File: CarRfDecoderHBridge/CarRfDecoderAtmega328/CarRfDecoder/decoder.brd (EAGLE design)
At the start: 98.7 x 80 mm, 54 parts, among them U2 RFM69CW, U3 MCP73831, U4 ATMEGA328P, U6 MIC5219 3.3V, Y1 16MHZ

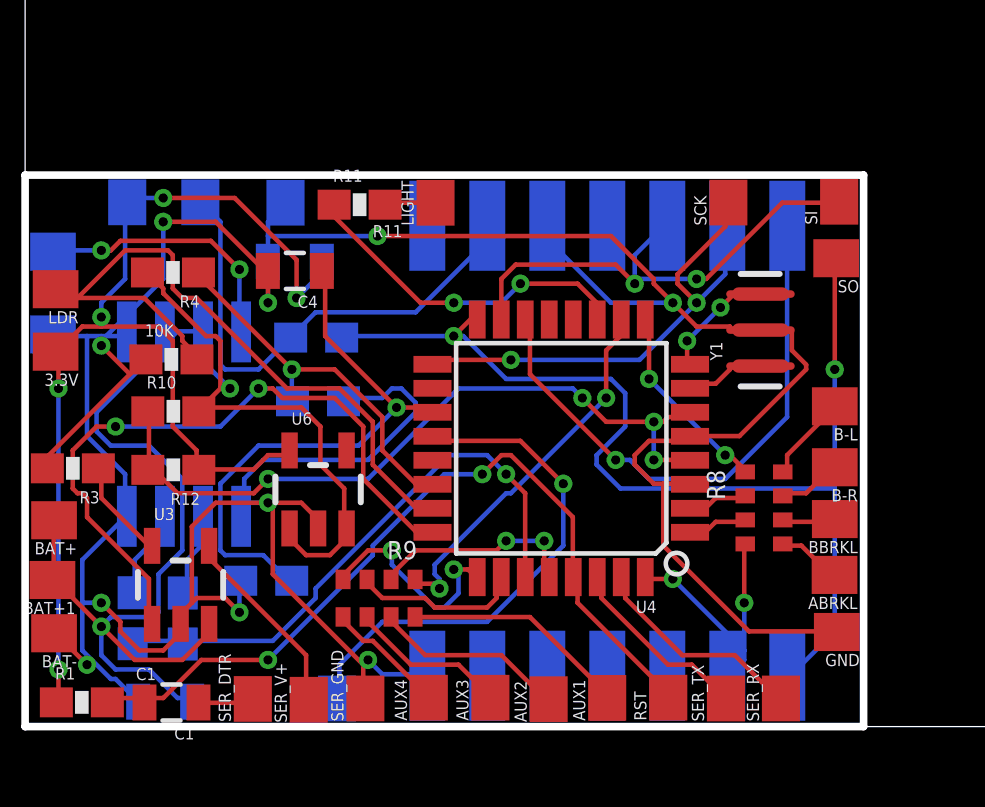
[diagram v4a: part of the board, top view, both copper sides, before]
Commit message: Change the pin to H-bridge to allow reverse control of the motor using A5
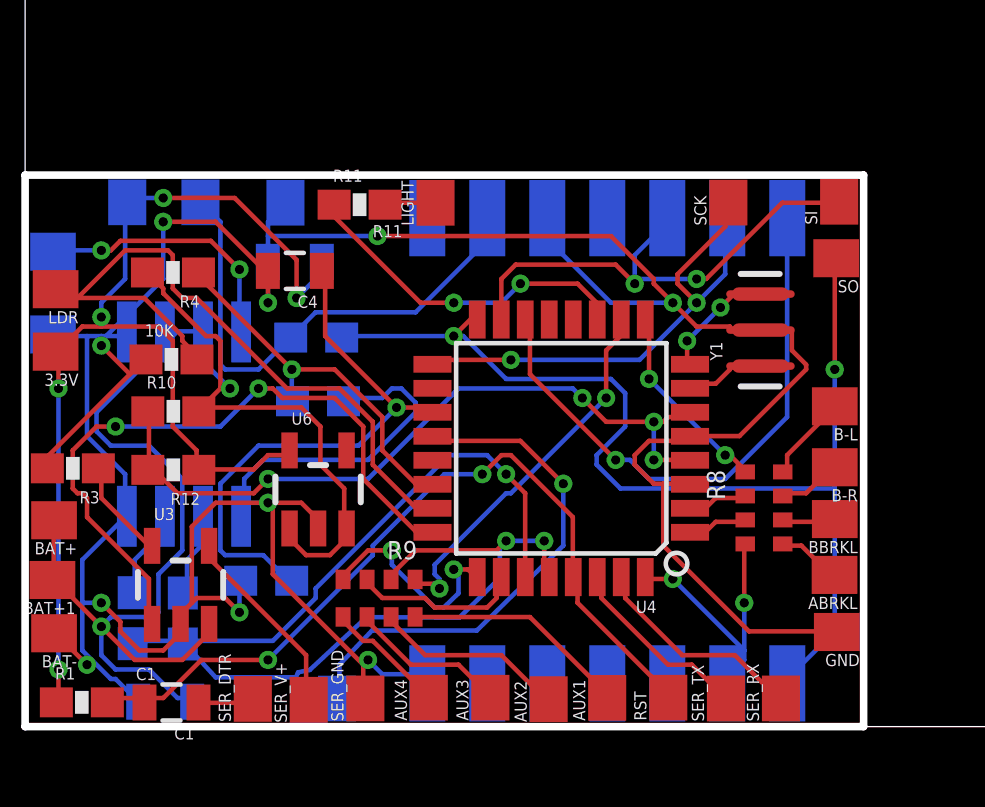
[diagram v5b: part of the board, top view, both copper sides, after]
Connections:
- net A4: no longer R6.1
- net A5: now also R6.1
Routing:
- net A5: track 7.00 -> 20.7 mm
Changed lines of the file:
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@@
 <wire x1="23.65375" y1="13.335" x2="22.86" y2="14.12875" width="0.1524" layer="1"/>
 <wire x1="24.765" y1="13.335" x2="23.65375" y2="13.335" width="0.1524" layer="1"/>
-<wire x1="18.7325" y1="16.66875" x2="18.6756" y2="16.6948" width="0.1524" layer="16"/>
+<wire x1="18.7325" y1="16.66875" x2="18.6756" y2="16.9488" width="0.1524" layer="16"/>
 <wire x1="24.765" y1="13.335" x2="24.765634375" y2="13.218053125" width="0.1524" layer="1"/>
 <wire x1="13.17625" y1="10.95375" x2="11.90625" y2="10.95375" width="0.1524" layer="16"/>
@@
 <wire x1="12.7" y1="2.2225" x2="13.17625" y2="1.74625" width="0.1524" layer="16"/>
 <wire x1="12.54125" y1="2.06375" x2="12.7" y2="2.2225" width="0.1524" layer="1"/>
-<wire x1="14.605" y1="1.74625" x2="14.6756" y2="1.6948" width="0.1524" layer="16"/>
+<wire x1="14.605" y1="1.74625" x2="14.6756" y2="1.4408" width="0.1524" layer="16"/>
 <wire x1="9.36625" y1="7.46125" x2="8.5725" y2="7.46125" width="0.1524" layer="16"/>
 <wire x1="8.5725" y1="7.46125" x2="8.4692625" y2="7.008784375" width="0.1524" layer="16"/>
@@
 <wire x1="19.20875" y1="8.09625" x2="17.78" y2="9.525" width="0.1524" layer="1"/>
 <wire x1="19.20875" y1="6.0325" x2="19.20875" y2="8.09625" width="0.1524" layer="16"/>
-<wire x1="16.66875" y1="3.4925" x2="19.20875" y2="6.0325" width="0.1524" layer="16"/>
-<wire x1="13.17625" y1="3.4925" x2="16.66875" y2="3.4925" width="0.1524" layer="16"/>
-<wire x1="11.7475" y1="2.06375" x2="13.17625" y2="3.4925" width="0.1524" layer="16"/>
+<wire x1="16.32493125" y1="3.201584375" x2="19.20875" y2="6.0325" width="0.1524" layer="16"/>
+<wire x1="12.83243125" y1="3.201584375" x2="16.32493125" y2="3.201584375" width="0.1524" layer="16"/>
+<wire x1="11.7475" y1="2.06375" x2="12.83243125" y2="3.201584375" width="0.1524" layer="16"/>
 <wire x1="11.7475" y1="0.9525" x2="11.7475" y2="2.06375" width="0.1524" layer="16"/>
 <wire x1="14.9225" y1="9.525" x2="14.84846875" y2="9.676678125" width="0.1524" layer="1"/>
@@
 <signal name="A4">
 <contactref element="U4" pad="27"/>
-<contactref element="R6" pad="1"/>
 <contactref element="R7" pad="1"/>
 <wire x1="6.50875" y1="2.8575" x2="4.92125" y2="2.8575" width="0.1524" layer="16"/>
 <wire x1="4.92125" y1="2.8575" x2="4.854525" y2="2.76374375" width="0.1524" layer="16"/>
-<wire x1="6.50875" y1="2.8575" x2="6.526196875" y2="2.753640625" width="0.1524" layer="16"/>
 <wire x1="17.93875" y1="7.77875" x2="17.93875" y2="5.08" width="0.1524" layer="1"/>
 <wire x1="17.30375" y1="8.41375" x2="17.93875" y2="7.77875" width="0.1524" layer="1"/>
@@
 <wire x1="6.6675" y1="2.8575" x2="9.525" y2="2.8575" width="0.1524" layer="16"/>
 <wire x1="17.93875" y1="5.08" x2="17.94106875" y2="4.984078125" width="0.1524" layer="1"/>
-<wire x1="6.6675" y1="2.8575" x2="6.526196875" y2="2.753640625" width="0.1524" layer="16"/>
 <via x="17.30375" y="8.41375" extent="1-16" drill="0.3048"/>
+<wire x1="6.50875" y1="2.8575" x2="6.6675" y2="2.8575" width="0" layer="19" extent="16-16"/>
 </signal>
 <signal name="A5">
@@
 <via x="17.30375" y="6.19125" extent="1-16" drill="0.3048"/>
 <via x="18.57375" y="6.19125" extent="1-16" drill="0.3048"/>
+<contactref element="R6" pad="1"/>
+<wire x1="6.526196875" y1="2.753640625" x2="6.601365625" y2="2.753640625" width="0.1524" layer="16"/>
+<wire x1="6.601365625" y1="2.753640625" x2="7.619225" y2="1.643584375" width="0.1524" layer="16"/>
+<wire x1="7.619225" y1="1.643584375" x2="10.296246875" y2="1.643584375" width="0.1524" layer="16"/>
+<wire x1="10.296246875" y1="1.643584375" x2="10.369796875" y2="1.80933125" width="0.1524" layer="16"/>
+<wire x1="10.369796875" y1="1.80933125" x2="10.75734375" y2="1.887346875" width="0.1524" layer="16"/>
+<wire x1="10.75734375" y1="1.887346875" x2="12.64968125" y2="3.64808125" width="0.1524" layer="16"/>
+<wire x1="12.64968125" y1="3.64808125" x2="15.742296875" y2="3.633371875" width="0.1524" layer="16"/>
+<wire x1="15.742296875" y1="3.633371875" x2="17.095715625" y2="4.957378125" width="0.1524" layer="16"/>
+<wire x1="17.095715625" y1="4.957378125" x2="17.095715625" y2="5.983215625" width="0.1524" layer="16"/>
+<wire x1="17.095715625" y1="5.983215625" x2="17.30375" y2="6.19125" width="0.1524" layer="16"/>
 </signal>
 <signal name="D7">
@@
 <wire x1="26.67" y1="16.66875" x2="26.67" y2="10.31875" width="0.1524" layer="16"/>
 <wire x1="18.0975" y1="13.49375" x2="17.94106875" y2="13.569278125" width="0.1524" layer="1"/>
-<wire x1="26.67" y1="16.66875" x2="26.6756" y2="16.6948" width="0.1524" layer="16"/>
+<wire x1="26.67" y1="16.66875" x2="26.6756" y2="16.9488" width="0.1524" layer="16"/>
 <via x="20.955" y="8.89" extent="1-16" drill="0.3048"/>
 </signal>
@@
 <wire x1="24.60625" y1="16.66875" x2="24.60625" y2="15.08125" width="0.1524" layer="16"/>
 <wire x1="14.9225" y1="12.22375" x2="14.84846875" y2="12.076678125" width="0.1524" layer="1"/>
-<wire x1="24.60625" y1="16.66875" x2="24.6756" y2="16.6948" width="0.1524" layer="16"/>
+<wire x1="24.60625" y1="16.66875" x2="24.6756" y2="16.9488" width="0.1524" layer="16"/>
 <wire x1="24.60625" y1="16.66875" x2="24.60625" y2="17.4625" width="0.1524" layer="1"/>
 <wire x1="23.01875" y1="15.08125" x2="24.60625" y2="16.66875" width="0.1524" layer="1"/>
@@
 <wire x1="22.5425" y1="16.66875" x2="21.59" y2="15.71625" width="0.1524" layer="16"/>
 <wire x1="17.145" y1="13.6525" x2="17.14106875" y2="13.569278125" width="0.1524" layer="1"/>
-<wire x1="22.5425" y1="16.66875" x2="22.6756" y2="16.6948" width="0.1524" layer="16"/>
+<wire x1="22.5425" y1="16.66875" x2="22.6756" y2="16.9488" width="0.1524" layer="16"/>
 <wire x1="26.51125" y1="17.4625" x2="28.2575" y2="17.4625" width="0.1524" layer="1"/>
 <wire x1="23.97125" y1="14.9225" x2="26.51125" y2="17.4625" width="0.1524" layer="1"/>
@@
 <wire x1="26.82875" y1="1.74625" x2="28.2575" y2="3.175" width="0.1524" layer="16"/>
 <wire x1="28.2575" y1="15.5575" x2="28.30476875" y2="15.612640625" width="0.1524" layer="1"/>
-<wire x1="26.82875" y1="1.74625" x2="26.6756" y2="1.6948" width="0.1524" layer="16"/>
+<wire x1="26.82875" y1="1.74625" x2="26.6756" y2="1.4408" width="0.1524" layer="16"/>
 <wire x1="15.875" y1="13.0175" x2="15.5575" y2="13.0175" width="0.1524" layer="16"/>
 <wire x1="17.30375" y1="11.58875" x2="15.875" y2="13.0175" width="0.1524" layer="16"/>
@@
 <wire x1="24.765" y1="1.74625" x2="25.24125" y2="2.2225" width="0.1524" layer="16"/>
 <wire x1="25.24125" y1="6.0325" x2="25.27383125" y2="6.089553125" width="0.1524" layer="1"/>
-<wire x1="24.765" y1="1.74625" x2="24.6756" y2="1.6948" width="0.1524" layer="16"/>
+<wire x1="24.765" y1="1.74625" x2="24.6756" y2="1.4408" width="0.1524" layer="16"/>
 <wire x1="22.86" y1="4.92125" x2="22.06625" y2="4.92125" width="0.1524" layer="1"/>
 <wire x1="25.24125" y1="2.54" x2="22.86" y2="4.92125" width="0.1524" layer="16"/>
 <wire x1="22.06625" y1="4.92125" x2="21.94106875" y2="4.984078125" width="0.1524" layer="1"/>
-<wire x1="25.24125" y1="2.54" x2="24.6756" y2="1.6948" width="0.1524" layer="16"/>
+<wire x1="25.24125" y1="2.54" x2="24.6756" y2="1.4408" width="0.1524" layer="16"/>
 <via x="25.24125" y="4.1275" extent="1-16" drill="0.3048"/>
 <via x="22.86" y="4.92125" extent="1-16" drill="0.3048"/>
@@
 <wire x1="10.95375" y1="13.81125" x2="14.2875" y2="13.81125" width="0.1524" layer="16"/>
 <wire x1="10.16" y1="13.0175" x2="10.95375" y2="13.81125" width="0.1524" layer="16"/>
-<wire x1="16.66875" y1="16.66875" x2="16.6756" y2="16.6948" width="0.1524" layer="16"/>
+<wire x1="16.66875" y1="16.66875" x2="16.6756" y2="16.9488" width="0.1524" layer="16"/>
 <wire x1="10.16" y1="13.0175" x2="10.121090625" y2="12.966375" width="0.1524" layer="16"/>
 </signal>
@@
 <wire x1="13.49375" y1="5.87375" x2="12.7" y2="5.87375" width="0.1524" layer="1"/>
 <wire x1="13.49375" y1="5.3975" x2="13.49375" y2="5.87375" width="0.1524" layer="16"/>
-<wire x1="14.9225" y1="3.96875" x2="13.49375" y2="5.3975" width="0.1524" layer="16"/>
-<wire x1="15.24" y1="3.96875" x2="14.9225" y2="3.96875" width="0.1524" layer="16"/>
-<wire x1="15.71625" y1="4.445" x2="15.24" y2="3.96875" width="0.1524" layer="16"/>
+<wire x1="14.912909375" y1="3.976753125" x2="13.49375" y2="5.3975" width="0.1524" layer="16"/>
+<wire x1="15.230409375" y1="3.976753125" x2="14.912909375" y2="3.976753125" width="0.1524" layer="16"/>
+<wire x1="15.71625" y1="4.445" x2="15.230409375" y2="3.976753125" width="0.1524" layer="16"/>
 <wire x1="15.71625" y1="5.08" x2="15.71625" y2="4.445" width="0.1524" layer="16"/>
 <wire x1="15.5575" y1="5.23875" x2="15.71625" y2="5.08" width="0.1524" layer="16"/>

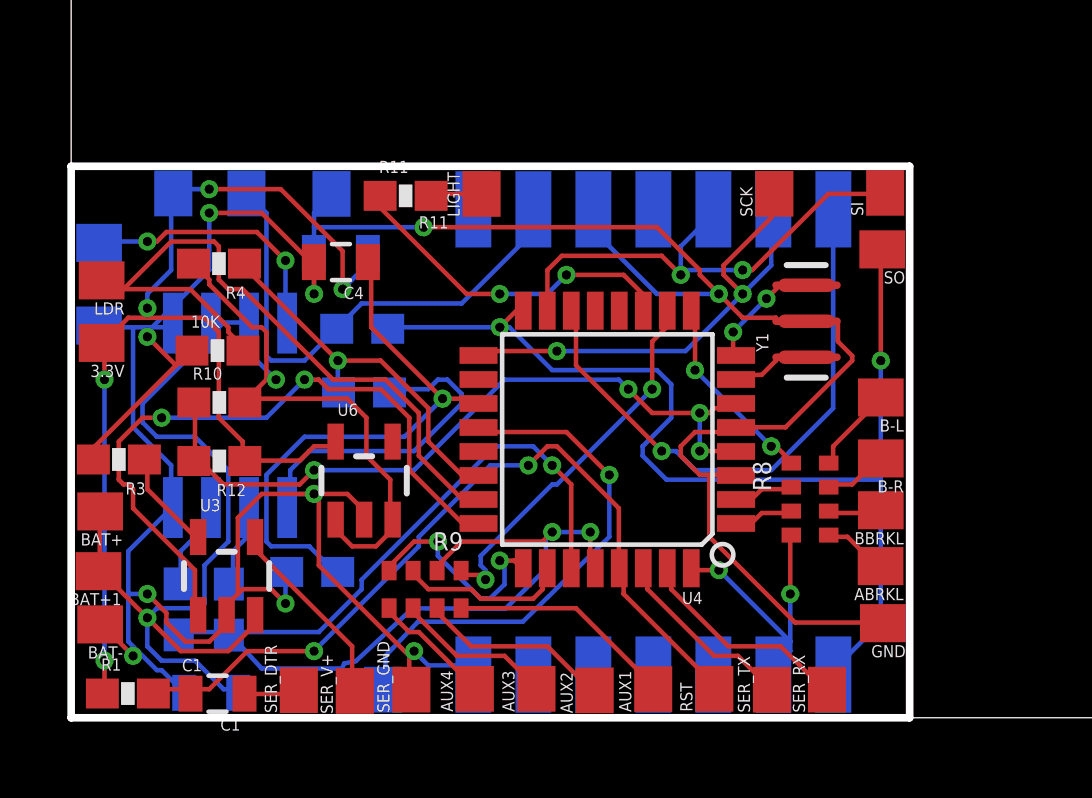
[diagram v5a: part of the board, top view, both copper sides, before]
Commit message: Fix R6 R7 bug. Disconnect motor from GND via R14
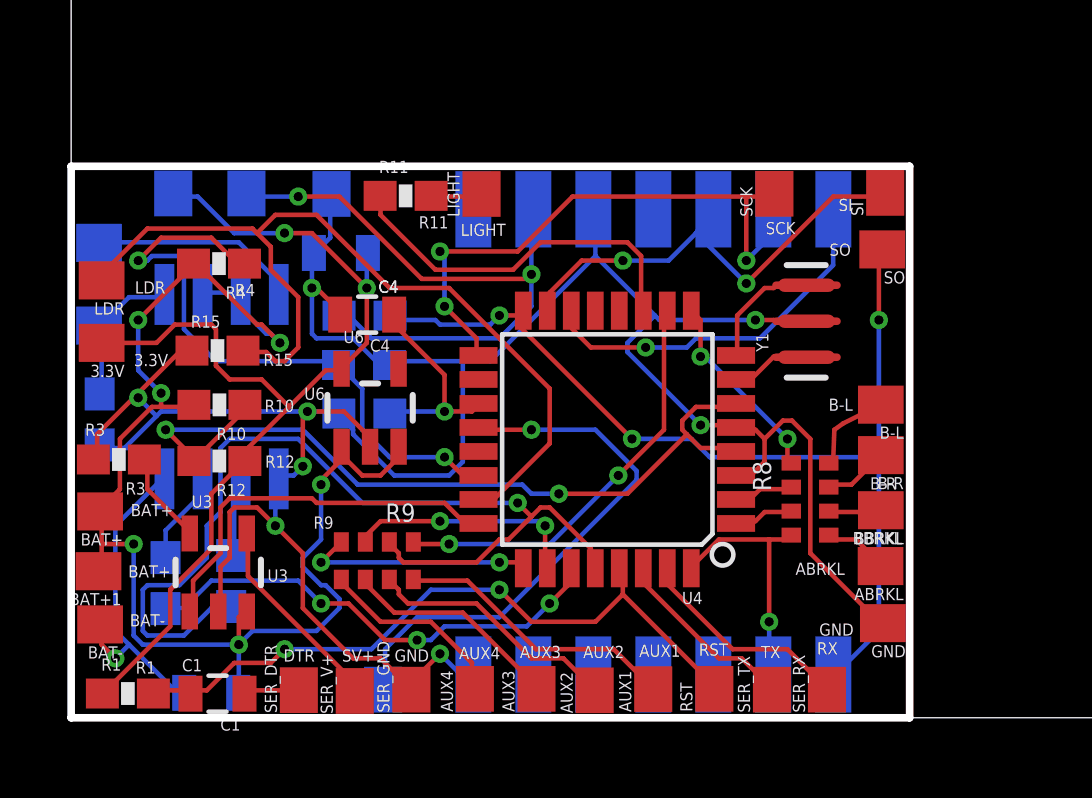
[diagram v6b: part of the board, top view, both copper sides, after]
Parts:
- added R14: 0, SparkFun-Resistors:0603-RES
- moved R2 5.56 mm to (11.0, 10.1)
- moved U6 2.44 mm to (11.2, 10.3)
- moved C4 1.96 mm to (11.1, 13.4)
- moved R9 1.86 mm to (11.5, 5.24)
- moved MDRIVER 1.00 mm to (6.29, 11.0)
- moved R7 0.98 mm to (4.42, 4.49)
- moved R6 0.96 mm to (6.61, 4.56)
- moved R5 0.92 mm to (11.0, 11.8)
- moved R13 0.44 mm to (11.1, 13.4)
- moved U3 0.30 mm to (6.17, 4.84)
- moved B-L 0.24 mm to (28.3, 10.4)
- moved B-R 0.11 mm to (28.3, 8.76)
- moved R10 0.08 mm to (6.21, 10.4), turned to 180 degrees
- renumbered 10K to R15
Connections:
- new net OA: MDRIVER.1, MOTORGND.1, R14.1
- net GND: now also R14.2; no longer MDRIVER.1, MOTORGND.1
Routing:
- net GND: track 121.6 -> 104.3 mm, vias 10 -> 9
- net A6: track 18.8 -> 7.02 mm
- net A5: track 20.7 -> 32.0 mm, vias 2 -> 1
- net A1: track 22.8 -> 13.0 mm, vias 2 -> 0
- net A7: track 12.6 -> 20.8 mm, vias 1 -> 2
- net SS: track 19.4 -> 12.6 mm
- net A0: track 24.2 -> 30.0 mm
- net OA: track 0.00 -> 4.95 mm
- net BAT+: track 49.5 -> 45.2 mm, vias 2 -> 6
- net N$5: track 27.5 -> 23.4 mm
- net N$1: track 17.2 -> 21.3 mm, vias 0 -> 2
- net VCC: track 38.1 -> 34.8 mm, vias 5 -> 2
- net MISO: track 37.2 -> 34.1 mm, vias 2 -> 3
- net A4: track 19.0 -> 16.0 mm, vias 1 -> 3
- net SCK: track 17.3 -> 20.2 mm, vias 2 -> 3
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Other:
- board text added: "2.56V"
- board text added: "3.3V"
- board text added: "ABRKL"
- board text added: "AUX1"
- board text added: "AUX2"
- board text added: "AUX3"
- board text added: "AUX4"
- board text added: "B-L"
- board text added: "B-R"
- board text added: "BAT+"
- board text added: "BAT-"
- board text added: "BBRKL"
- board text added: "C2"
- board text added: "C4"
- board text added: "DTR"
- board text added: "GND"
- board text added: "LDR"
- board text added: "LIGHT"
- board text added: "MDRIVER"
- board text added: "MOTOR"
- board text added: "MT-GND"
- board text added: "R1"
- board text added: "R10"
- board text added: "R12"
- board text added: "R13"
- board text added: "R14"
- board text added: "R15"
- board text added: "R2"
- board text added: "R3"
- board text added: "R4"
- board text added: "R5"
- board text added: "R6"
- board text added: "R7"
- board text added: "R9"
- board text added: "RST"
- board text added: "RX"
- board text added: "SCK"
- board text added: "SI"
- board text added: "SO"
- board text added: "SV+"
- board text added: "TX"
- board text added: "U3"
- board text added: "U6"
- board text added: "VJ"
